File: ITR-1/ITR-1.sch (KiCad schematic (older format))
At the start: 4 parts, among them K1 кнопка

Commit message: схема организации питания
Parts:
- added C1, C2: Конденсатор_керамический, N_RLC:Конденсатор_SMD_IEC_0805, symbol elements:Конденсатор_керамический
- added C3: Конденсатор_керамический, N_RLC:Конденсатор_SMD_0603_pnp, symbol elements:Конденсатор_керамический
- added C4, C5: Конденсатор_керамический, N_RLC:Конденсатор_SMD_IEC_0603, symbol elements:Конденсатор_керамический
- added DD1: Микросхема_заряда_MCP73831T-2ACI_OT, N_G:SOT-23-5_pnp, symbol elements_2020:Микросхема_заряда_MCP73831T-2ACI_OT
- added G2: ИОП_LM4040BIM3-2.5_NOPB, N_VD_HL:Транзистор_IRLML6344TR_SOT-23, symbol elements_2020:ИОП_LM4040BIM3-2.5_NOPB
- added R1, R10, R11, R12, R2, R3, R4, R5, R6, R7, R8, R9: Резистор_0,065Вт, N_RLC:Резистор_SMD_0603_0,065_Вт, symbol elements:Резистор_0,065Вт
- added VD1: Диоды_шоттки_BAR43CFILM, N_VD_HL:Транзистор_IRLML6344TR_SOT-23, symbol elements_2020:Диоды_шоттки_BAR43CFILM
- added VT1, VT4: Транзистор_полевой_P-канал(IRLML2246TRPBF), N_VD_HL:Транзистор_IRLML6344TR_SOT-23, symbol elements:Транзистор_полевой_P-канал(IRLML2246TRPBF)
- added VT2, VT3: Транзистор_полевой_N-IRLML6344TR, N_VD_HL:Транзистор_IRLML6344TR_SOT-23, symbol elements:Транзистор_полевой_N-IRLML6344TR
- added X1: Клеммник_х2, symbol elements:Клеммник_х2
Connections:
- net GND: now reaches G1.1 (GND)
- net GND: now also C1.2, C2.2, C4.2, C5.2, DD1.2 (VSS/GND), G2.2, R11.2, R2.2, R5.2, R7.2, VT2.2, X1.2
- net 3V3: now reaches G1.2 (3В3)
- net 3V3: now also G1.4 (BOT), C5.1
- net BAT.LOAD: now reaches G1.3 (4...15_В)
- net BAT.LOAD: now also C4.1, R10.1, R12.1, VT1.3
- new net: DD1.1 (STAT), R8.2
- new net: DD1.5 (PROG), R7.1
- new net: R1.2, VD1.1, VD1.2, VT1.1, VT2.3
- new net: R2.1, R3.2, VT2.1
- new net: R5.1, R6.2, VT4.1
- new net: R9.2, VD1.3, X1.1
- new net 2V5.REF: G2.1, R12.2
- new net BAT.IN: C2.1, DD1.3 (VBAT), R1.1, VT1.2
- new net BAT.MEASURE: R10.2, R11.1
- new net BUTT.TURN: R9.1
- new net CHARGE.MODE: R8.1
- new net SELF.TURN: R3.1
- new net U.IN: VT4.3
- new net U.PROTECT: C1.1, DD1.4 (VDD), R6.1, VT4.2
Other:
- note added: "-нажатие кнопки открывает транзистор питания\n-на линии SELF.TURN МК должен выставить высокий уровень для самоподхвата\n-на лии BUTT.TURN МК в режиме PULL-UP видит состояние кнопки включения"
- note added: "~~300 мА"
- note added: "включение питания с самоподхватом"
- note added: "защита от переполюсовки"
- moved on the sheet: A1, G1, HL1, K1

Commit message: закончена схема, начата трассировка питания
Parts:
- removed C3: Конденсатор_керамический, N_RLC:Конденсатор_SMD_0603_pnp, symbol elements:Конденсатор_керамический
- removed K1: кнопка, N_X:Кнопка_FSMSM, symbol elements:кнопка
- removed X1: Клеммник_х2, symbol elements:Клеммник_х2
- added FU1: Предохранитель_MF-MSMF030, N_RLC:Предохранитель_SMD_1812, symbol elements:Предохранитель
- added K1: Кнопка_KLS7-TS5401-1.35-250-T, N_X:Кнопка_KLS7-TS5401, symbol elements_2020:Кнопка_KLS7-TS5401-1.35-250-T
- added R13, R14, R15, R16, R17, R18, R19, R20, R21, R22, R23, R24, R25, R26: Резистор_0,065Вт, N_RLC:Резистор_SMD_0603_0,065_Вт, symbol elements:Резистор_0,065Вт
- added VD2, VD3, VD4: Стабилитрон_BZV55C2V7, N_VD_HL:SOD-80, symbol elements_2020:Стабилитрон_1N5352BRLG_вертикальный
- added VD5: Стабилитрон_BZV55-C3V9, N_VD_HL:SOD-80, symbol elements_2020:Стабилитрон_1N5352BRLG_вертикальный
- added VT5: Транзистор_полевой_N-IRLML6344TR, N_VD_HL:Транзистор_IRLML6344TR_SOT-23, symbol elements:Транзистор_полевой_N-IRLML6344TR
- added X1, X2: отверстие_под_пайку, N_X:ОтверстиеD1.2, symbol elements:отверстие_под_пайку
- added XS1, XS2: Клеммник_х3, N_X:jack_ST-033, symbol elements:Клеммник_х3
- R4: INFO (none) -> 240 Ом; Номинал 100 Ом -> (none)
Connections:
- net 2V5.REF: now also A1.6 (IO34)
- net 3V3: now also A1.2 (3V3), HL1.1, HL1.3, R18.2, R26.2, VD5.2
- net BAT.IN: now also FU1.1, X2.1; no longer C2.1, DD1.3 (VBAT), R1.1, VT1.2
- net BAT.MEASURE: now also A1.7 (IO35)
- net BUTT.TURN: now also A1.11 (IO26)
- net CHARGE.MODE: now also A1.13 (IO14)
- net GND: now also A1.1 (GND), A1.15 (GND), A1.38 (GND), A1.39 (GND), VT3.2, K1.3, K1.4, R14.1, R15.1, VD2.1, VD3.1, VD4.1, VD5.1, VT5.2, X1.1, XS2.3
- net SELF.TURN: now also A1.9 (IO33)
- net U.IN: now also XS2.1
- net BOOT: now reaches A1.25 (IO(ноль)_BOOT)
- net BOOT: now also R24.1
- net LED.RED: now reaches A1.29 (IO5)
- net LED.RED: now also R13.2
- net RESET: now reaches A1.3 (EN)
- net RESET: now also R25.2
- net LED.GREEN: now reaches A1.31 (IO19)
- net LED.GREEN: now also R4.2
- net UART.RX: now reaches A1.34 (RXD0)
- net UART.RX: now also R22.1
- net UART.TX: now reaches A1.35 (TXD0)
- net UART.TX: now also R23.1
- net at HL1.2: now also R17.1
- net at HL1.4: now also R16.1
- net at VT3.1: now also R4.1, R14.2
- net at VT3.3: now also R16.2
- net EXT.BUTT: now reaches R9.2, VD1.3
- net EXT.BUTT: now also XS2.2
- new net: C2.1, DD1.3 (VBAT), FU1.2, R1.1, VT1.2
- new net: R13.1, R15.2, VT5.1
- new net: R17.2, VT5.3
- new net: K1.1, K1.2, R25.1, R26.1
- new net: R18.1, R21.1, R24.2, VD2.2
- new net: R20.1, R23.2, VD3.2
- new net: R19.1, R22.2, VD4.2
- new net OUT.BOOT: R21.2, XS1.3
- new net OUT.RX: R19.2, XS1.1
- new net OUT.TX: R20.2, XS1.2
- no-connect marks 0 -> 9
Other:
- note added: "ПОДКЛЮЧЕНИЕ ПРОГРАММИРОВАНИЯ"
- note added: "СХЕМА СБРОСА"
- moved on the sheet: A1, C1, C2, C4, C5, DD1, G1, G2, HL1, R1, R10, R11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

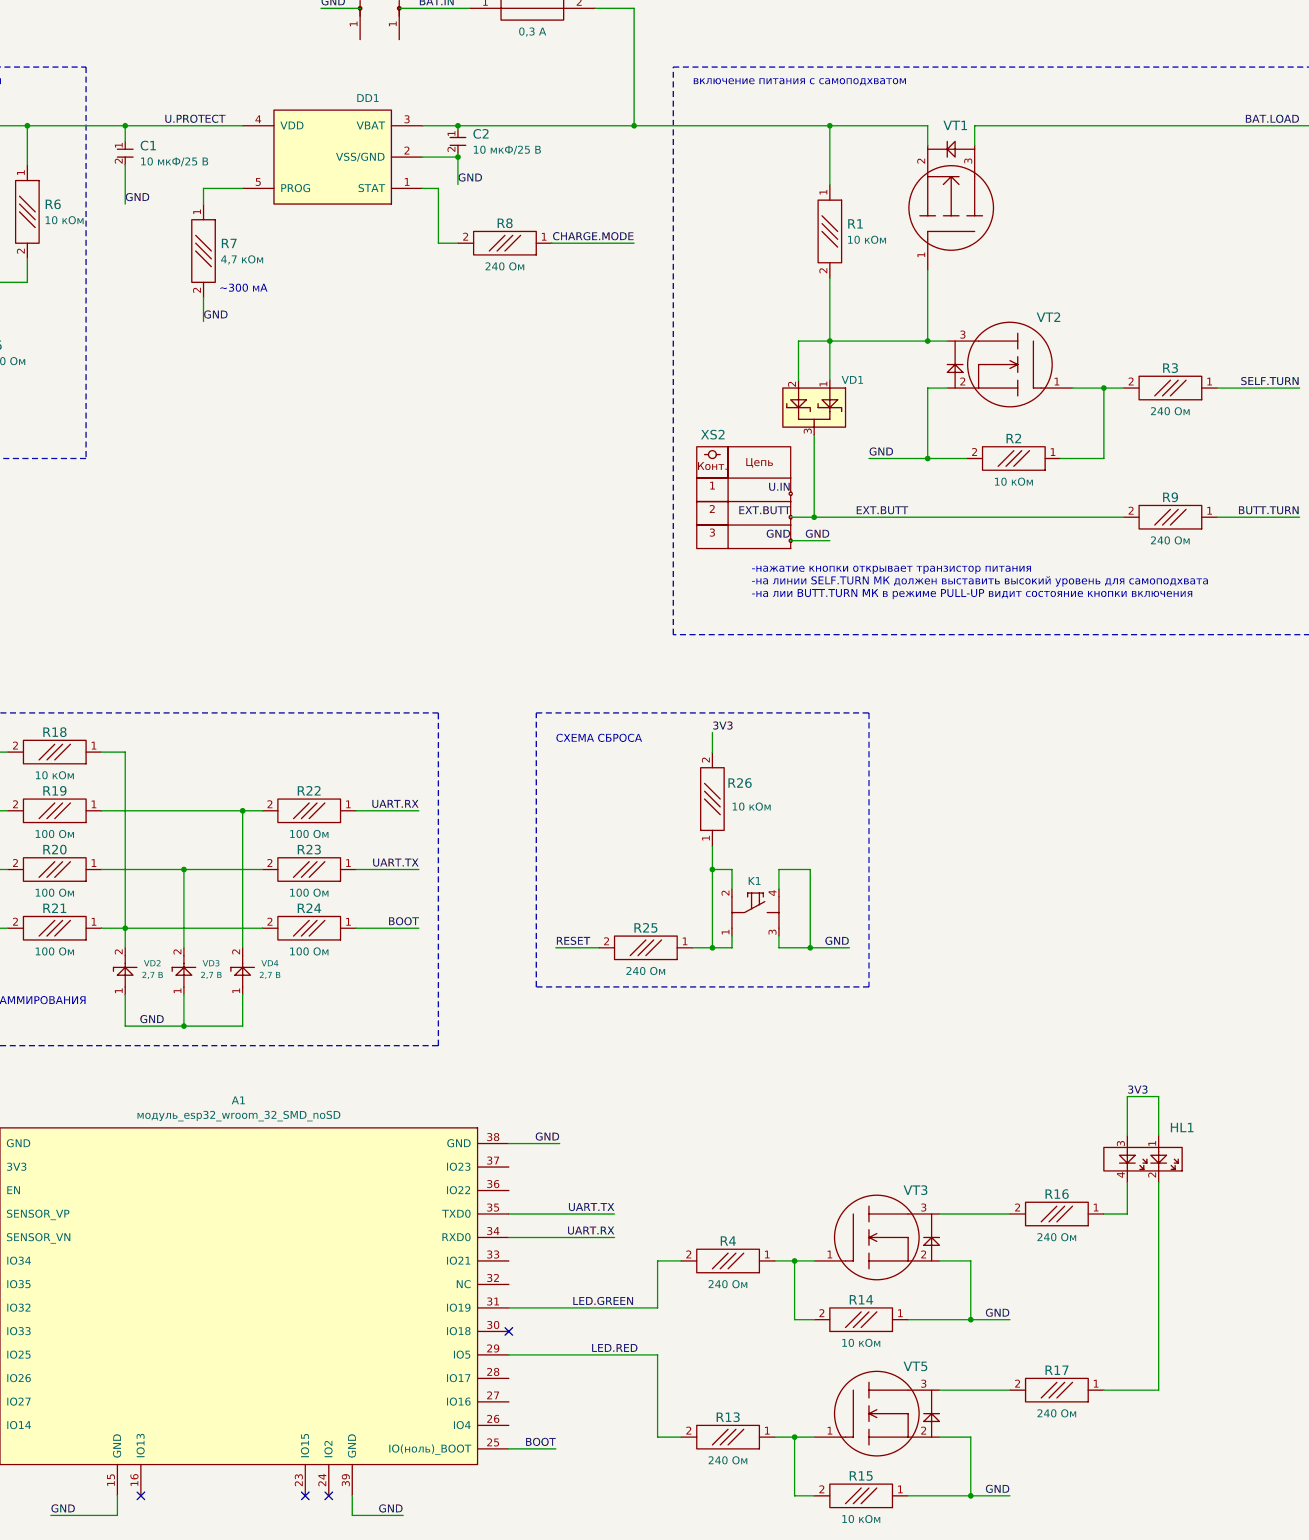
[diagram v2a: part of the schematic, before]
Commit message: подготовлена трассировка питания, упрощена схема подключения периферии
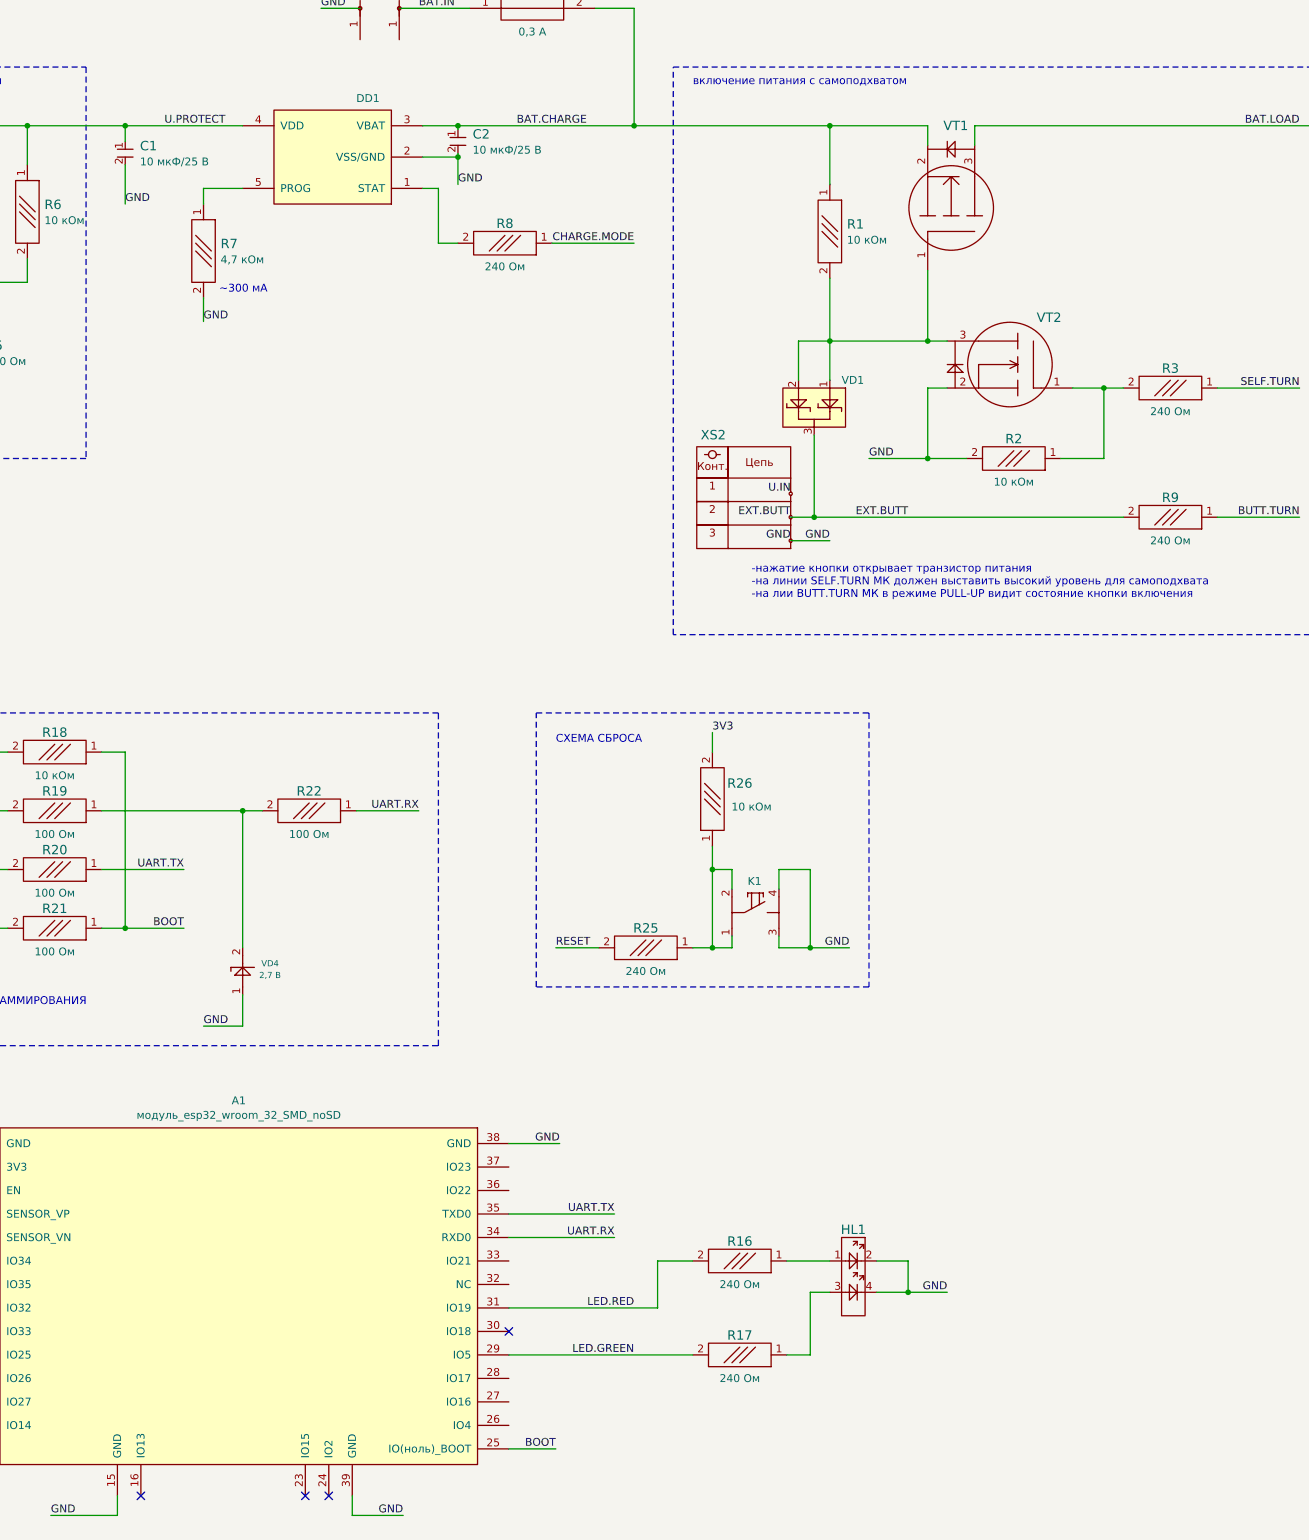
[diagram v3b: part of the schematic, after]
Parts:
- removed R13, R14, R15, R23, R24, R4: Резистор_0,065Вт, N_RLC:Резистор_SMD_0603_0,065_Вт, symbol elements:Резистор_0,065Вт
- removed VD2, VD3: Стабилитрон_BZV55C2V7, N_VD_HL:SOD-80, symbol elements_2020:Стабилитрон_1N5352BRLG_вертикальный
- removed VT3, VT5: Транзистор_полевой_N-IRLML6344TR, N_VD_HL:Транзистор_IRLML6344TR_SOT-23, symbol elements:Транзистор_полевой_N-IRLML6344TR
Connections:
- net 3V3: no longer HL1.1, HL1.3
- net BOOT: now also R18.1, R21.1
- net GND: now also HL1.2, HL1.4
- net LED.GREEN: now also A1.29 (IO5), R17.2; no longer A1.31 (IO19)
- net LED.RED: now also A1.31 (IO19), R16.2; no longer A1.29 (IO5)
- net UART.TX: now also R20.1
- net at R17.1: now also HL1.3; no longer HL1.2
- net at R16.1: now also HL1.1; no longer HL1.4
- net BAT.CHARGE: now reaches C2.1, DD1.3 (VBAT), FU1.2, R1.1, VT1.2
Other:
- moved on the sheet: HL1, R16, R17

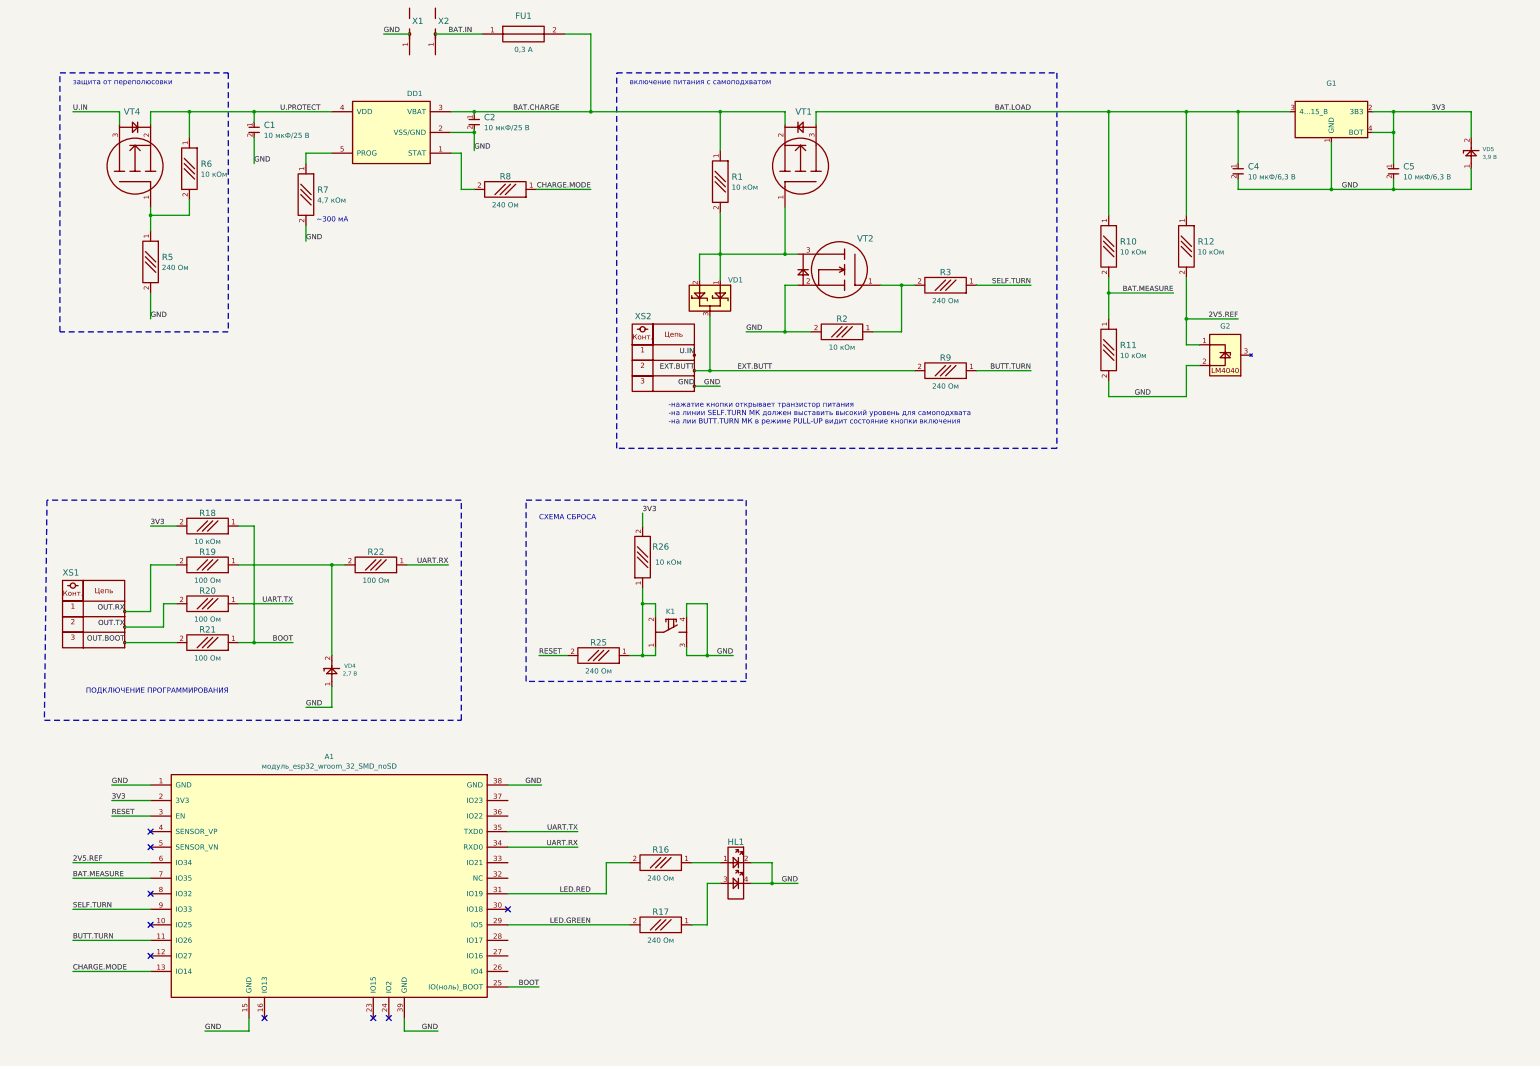
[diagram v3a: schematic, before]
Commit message: обновлены посадочные места и схема питания
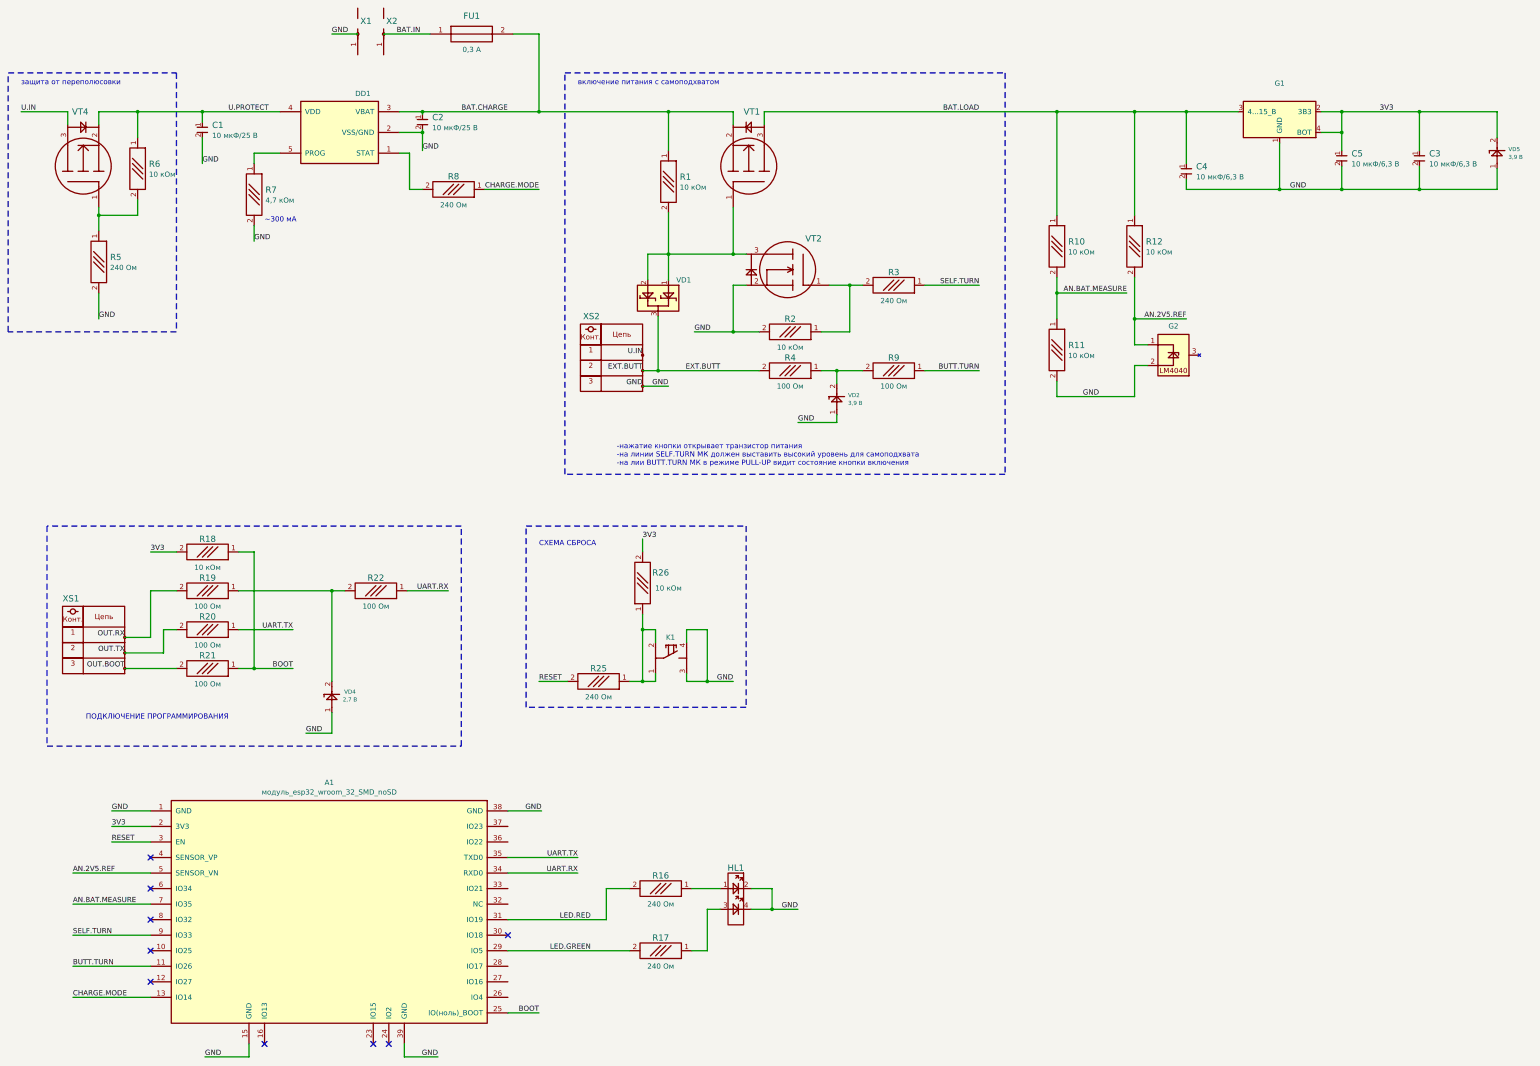
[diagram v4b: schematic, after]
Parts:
- added C3: Конденсатор_керамический, N_RLC:Конденсатор_SMD_0603_pnp, symbol elements:Конденсатор_керамический
- added R4: Резистор_0,065Вт, N_RLC:Резистор_SMD_0603_0,065_Вт, symbol elements:Резистор_0,065Вт
- added VD2: Стабилитрон_BZV55-C3V9, N_VD_HL:SOD-80, symbol elements_2020:Стабилитрон_1N5352BRLG_вертикальный
- C5: footprint N_RLC:Конденсатор_SMD_IEC_0603 -> N_RLC:Конденсатор_SMD_0603_pnp
- R9: INFO 240 Ом -> 100 Ом
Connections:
- net 3V3: now also C3.1
- net EXT.BUTT: now also R4.2; no longer R9.2
- net GND: now also C3.2, VD2.1
- net AN.2V5.REF: now reaches A1.5 (SENSOR_VN)
- net AN.2V5.REF: now also G2.1, R12.2
- removed net 2V5.REF: A1.6 (IO34), G2.1, R12.2
- net BAT.MEASURE renamed AN.BAT.MEASURE
- new net: R4.1, R9.2, VD2.2
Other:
- moved on the sheet: A1, C1, C2, C4, C5, DD1, FU1, G1, G2, HL1, K1, R1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
